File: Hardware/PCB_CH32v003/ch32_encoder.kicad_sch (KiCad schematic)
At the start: 25 parts, among them J1 Conn_01x03_Pin, J2 Conn_01x03_Pin, J3 Conn_01x04_Pin, Q1 2N7002K, U1 XC6206PxxxMR, U2 MT6701CT, U3 GD32F130F4P6TR

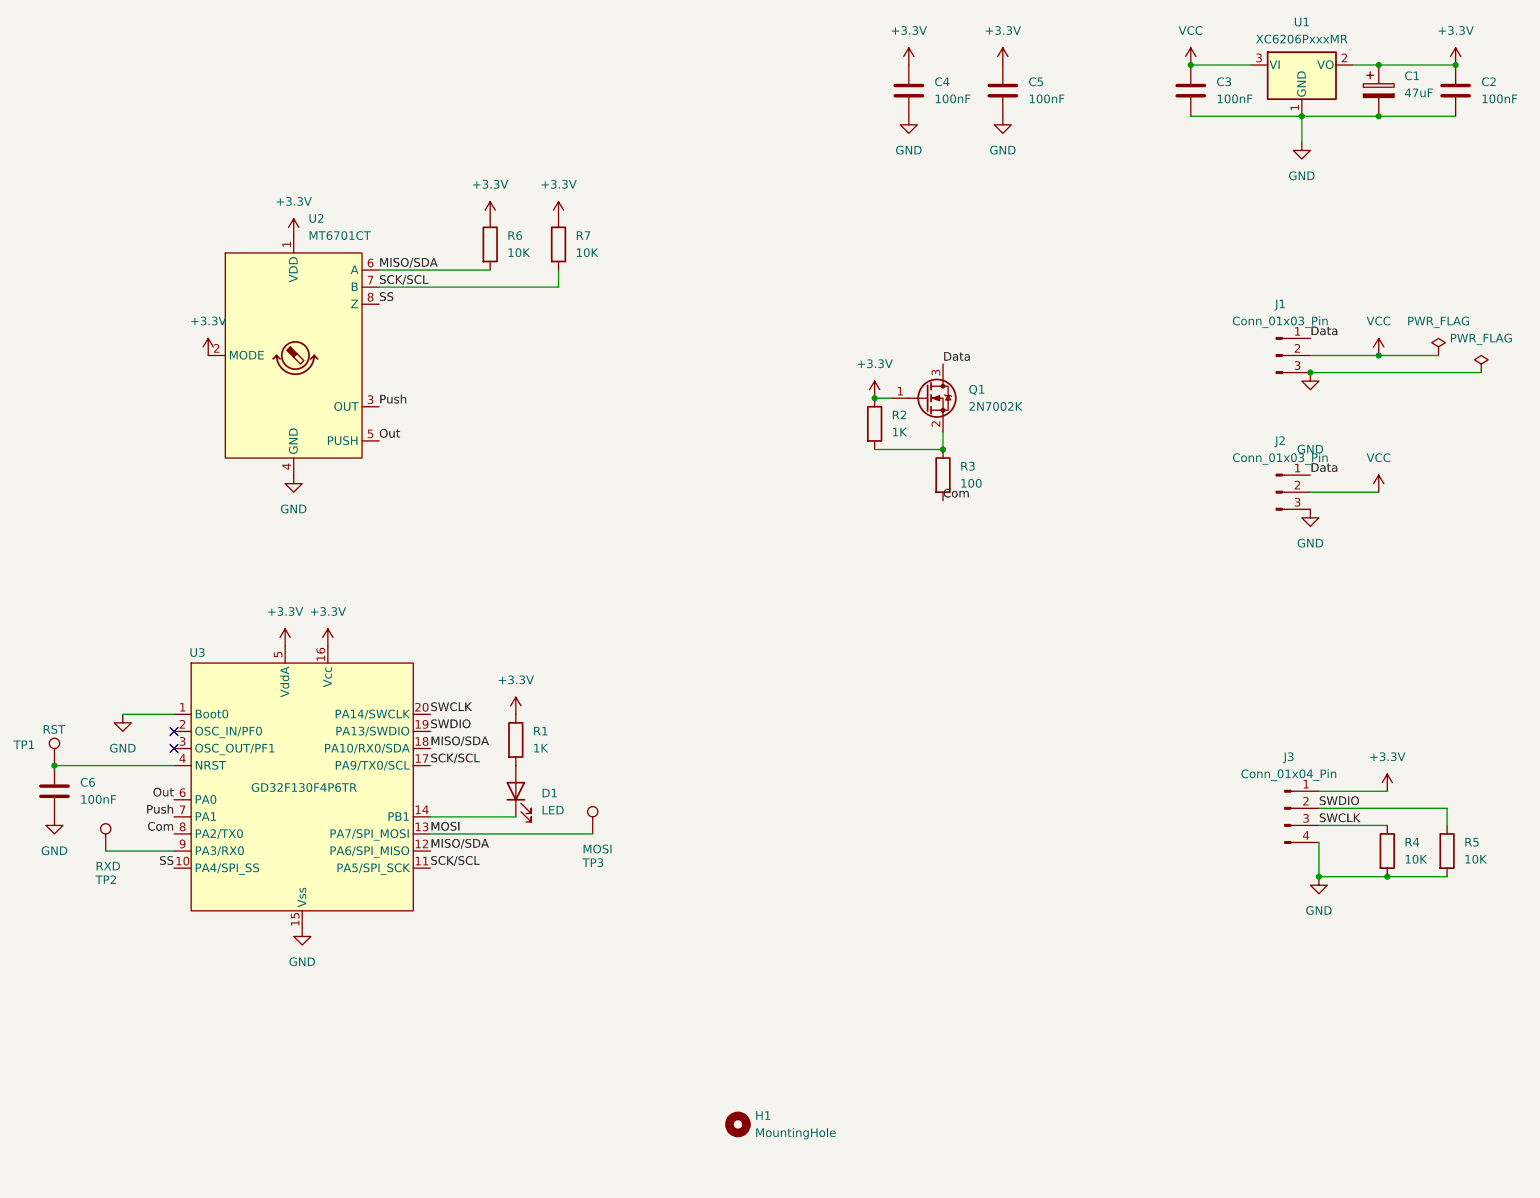
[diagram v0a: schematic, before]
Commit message: Added PCB for CH32V003, which is a bit cheaper. New revision of GD32F130 PCB.
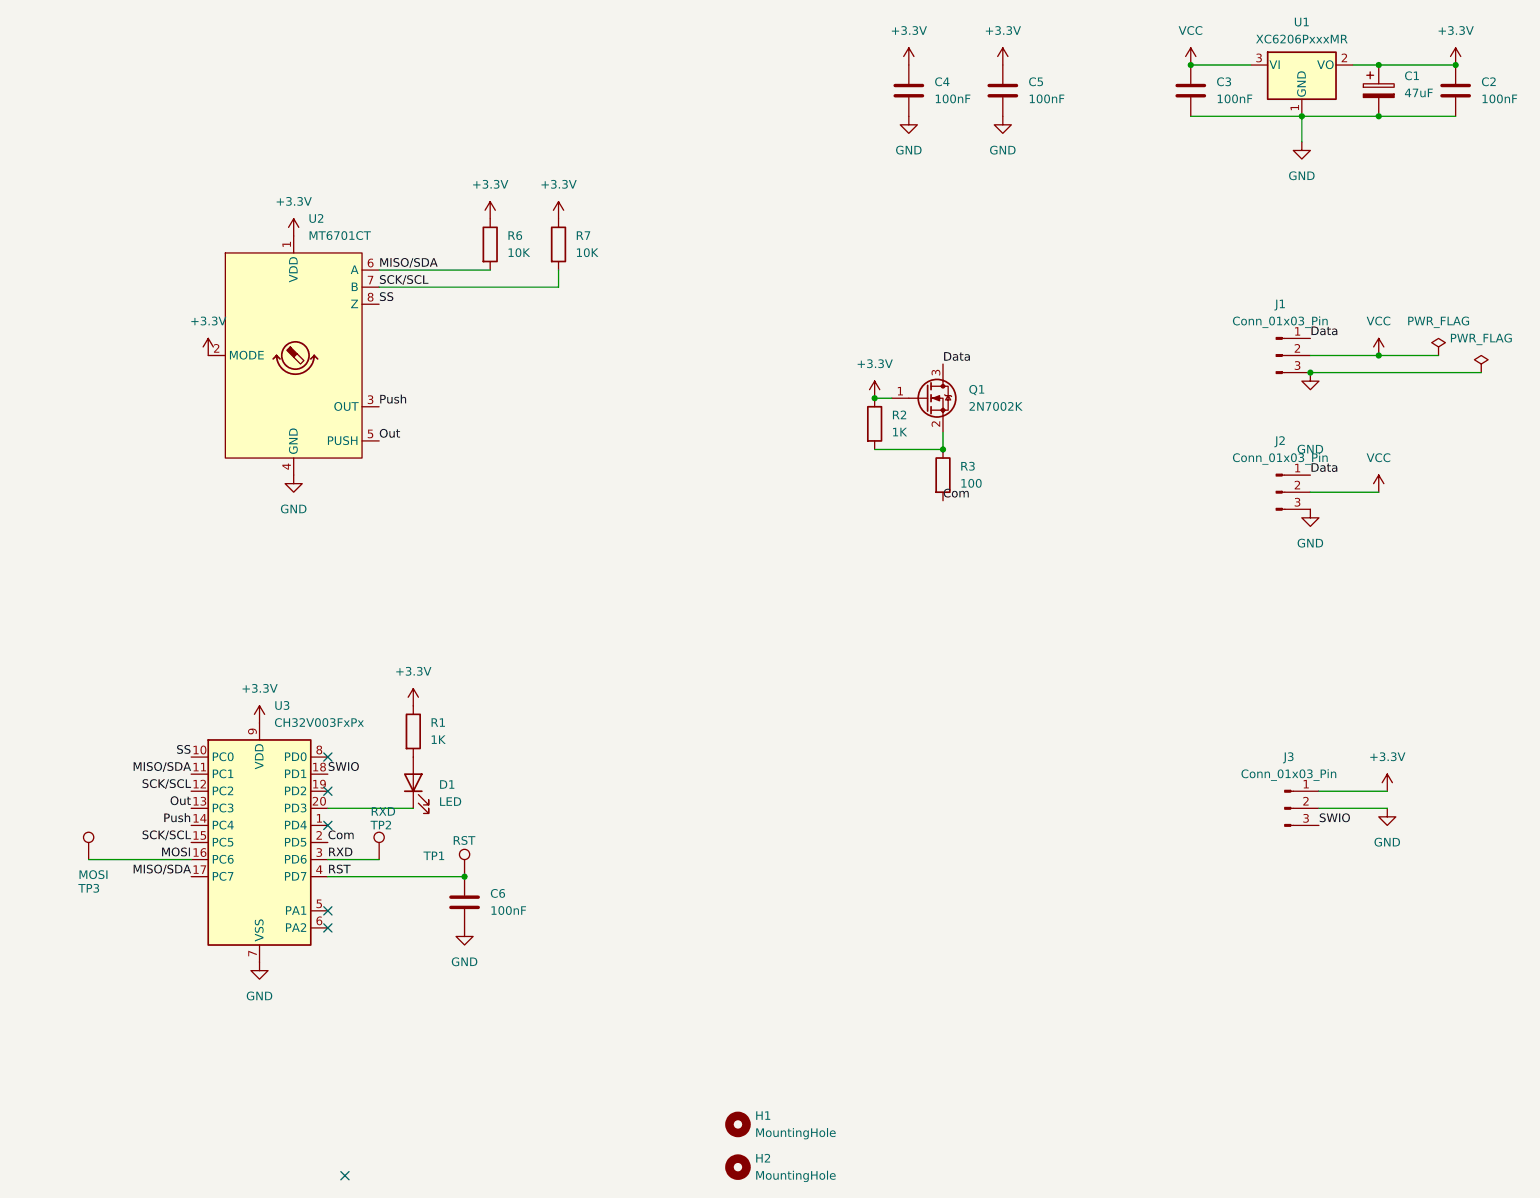
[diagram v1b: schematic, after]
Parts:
- removed J3: Conn_01x04_Pin, Connector_PinHeader_2.54mm:PinHeader_1x04_P2.54mm_Vertical, symbol Connector:Conn_01x04_Pin
- removed R4, R5: 10K, Resistor_SMD:R_0603_1608Metric_Pad0.98x0.95mm_HandSolder, symbol Device:R
- removed U3: GD32F130F4P6TR, Package_SO:TSSOP-20_4.4x6.5mm_P0.65mm, symbol My_Library:GD32F130F4P6TR
- added H2: MountingHole, MountingHole:MountingHole_2.2mm_M2_DIN965, symbol Mechanical:MountingHole
- added J3: Conn_01x03_Pin, Connector_PinHeader_2.54mm:PinHeader_1x03_P2.54mm_Vertical, symbol Connector:Conn_01x03_Pin
- added U3: CH32V003FxPx, Package_SO:TSSOP-20_4.4x6.5mm_P0.65mm, symbol MCU_WCH_CH32V0:CH32V003FxPx
- C1: footprint Capacitor_Tantalum_SMD:CP_EIA-1608-10_AVX-L_Pad1.25x1.05mm_HandSolder -> Capacitor_Tantalum_SMD:CP_EIA-3216-18_Kemet-A_Pad1.58x1.35mm_HandSolder
- C3: footprint Capacitor_SMD:C_0603_1608Metric -> Capacitor_SMD:C_0603_1608Metric_Pad1.08x0.95mm_HandSolder
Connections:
- net +3.3V: now also J3.1 (Pin_1), U3.9 (VDD)
- net Com: now also U3.2 (PD5)
- net GND: now also J3.2 (Pin_2), U3.7 (VSS)
- net MISO/SDA: now also U3.11 (PC1), U3.17 (PC7)
- net MOSI: now also U3.16 (PC6)
- net Out: now also U3.13 (PC3)
- net Push: now also U3.14 (PC4)
- net SCK/SCL: now also U3.12 (PC2), U3.15 (PC5)
- net SS: now also U3.10 (PC0)
- net at D1.1 (K): now also U3.20 (PD3)
- net RST: now reaches C6.1, TP1.1
- net RST: now also U3.4 (PD7)
- net RXD: now reaches TP2.1
- net RXD: now also U3.3 (PD6)
- new net SWIO: J3.3 (Pin_3), U3.18 (PD1)
- no-connect marks 2 -> 6
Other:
- moved on the sheet: C6, D1, R1, TP1, TP2, TP3

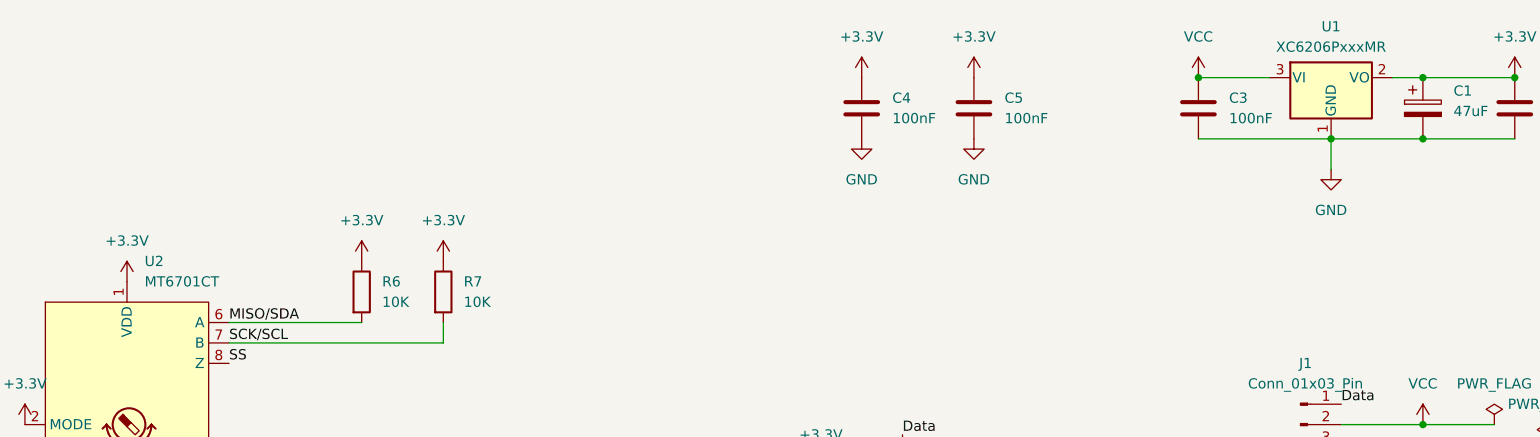
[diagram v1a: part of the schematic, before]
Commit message: Updated 3.3V regulator with HT7533S that supports 12V input. / Mentioned AS5600 compatibility.
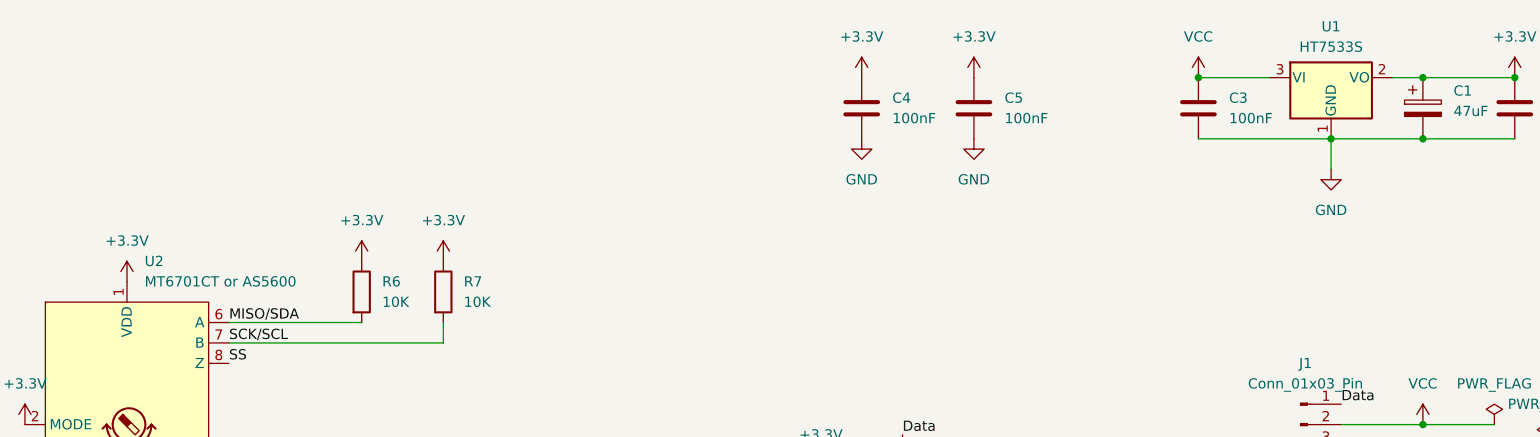
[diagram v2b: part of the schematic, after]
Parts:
- U1: value XC6206PxxxMR -> HT7533S
- U2: value MT6701CT -> MT6701CT or AS5600
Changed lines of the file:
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@@
 			)
 		)
-		(property "Value" "MT6701CT"
+		(property "Value" "MT6701CT or AS5600"
 			(at 93.6341 52.07 0)
 			(effects
@@
 			)
 		)
-		(property "Value" "XC6206PxxxMR"
+		(property "Value" "HT7533S"
 			(at 241.3 22.86 0)
 			(effects

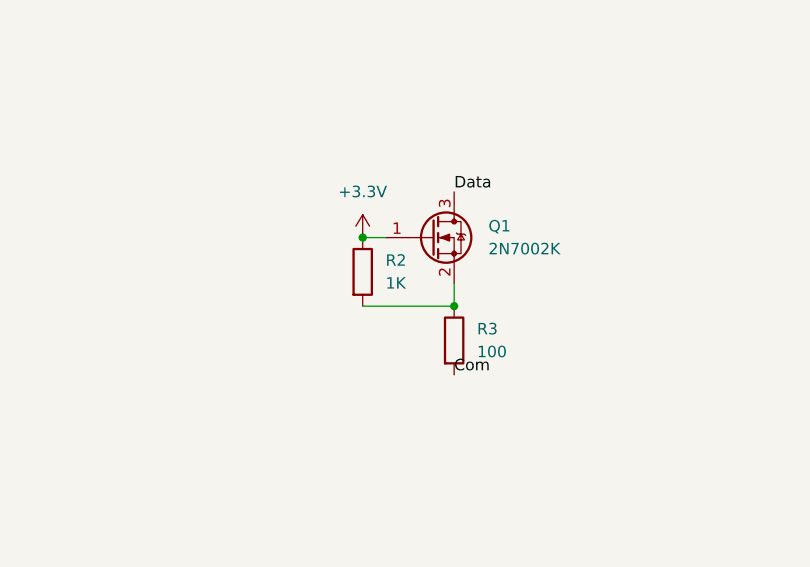
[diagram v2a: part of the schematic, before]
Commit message: Fixed R2 resistor value
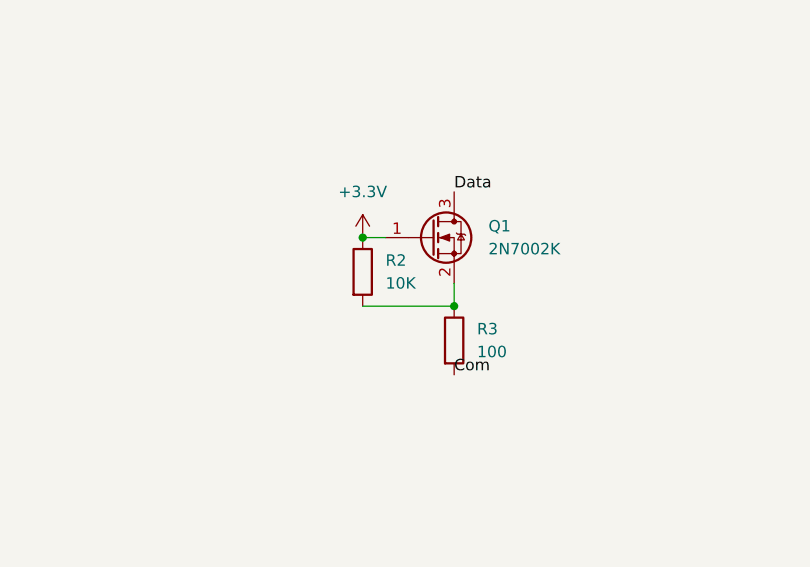
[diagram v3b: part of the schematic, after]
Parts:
- R2: value 1K -> 10K
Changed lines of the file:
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@@
 			)
 		)
-		(property "Value" "1K"
+		(property "Value" "10K"
 			(at 180.34 81.2799 0)
 			(effects
